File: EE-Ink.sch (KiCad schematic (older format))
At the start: 12 parts

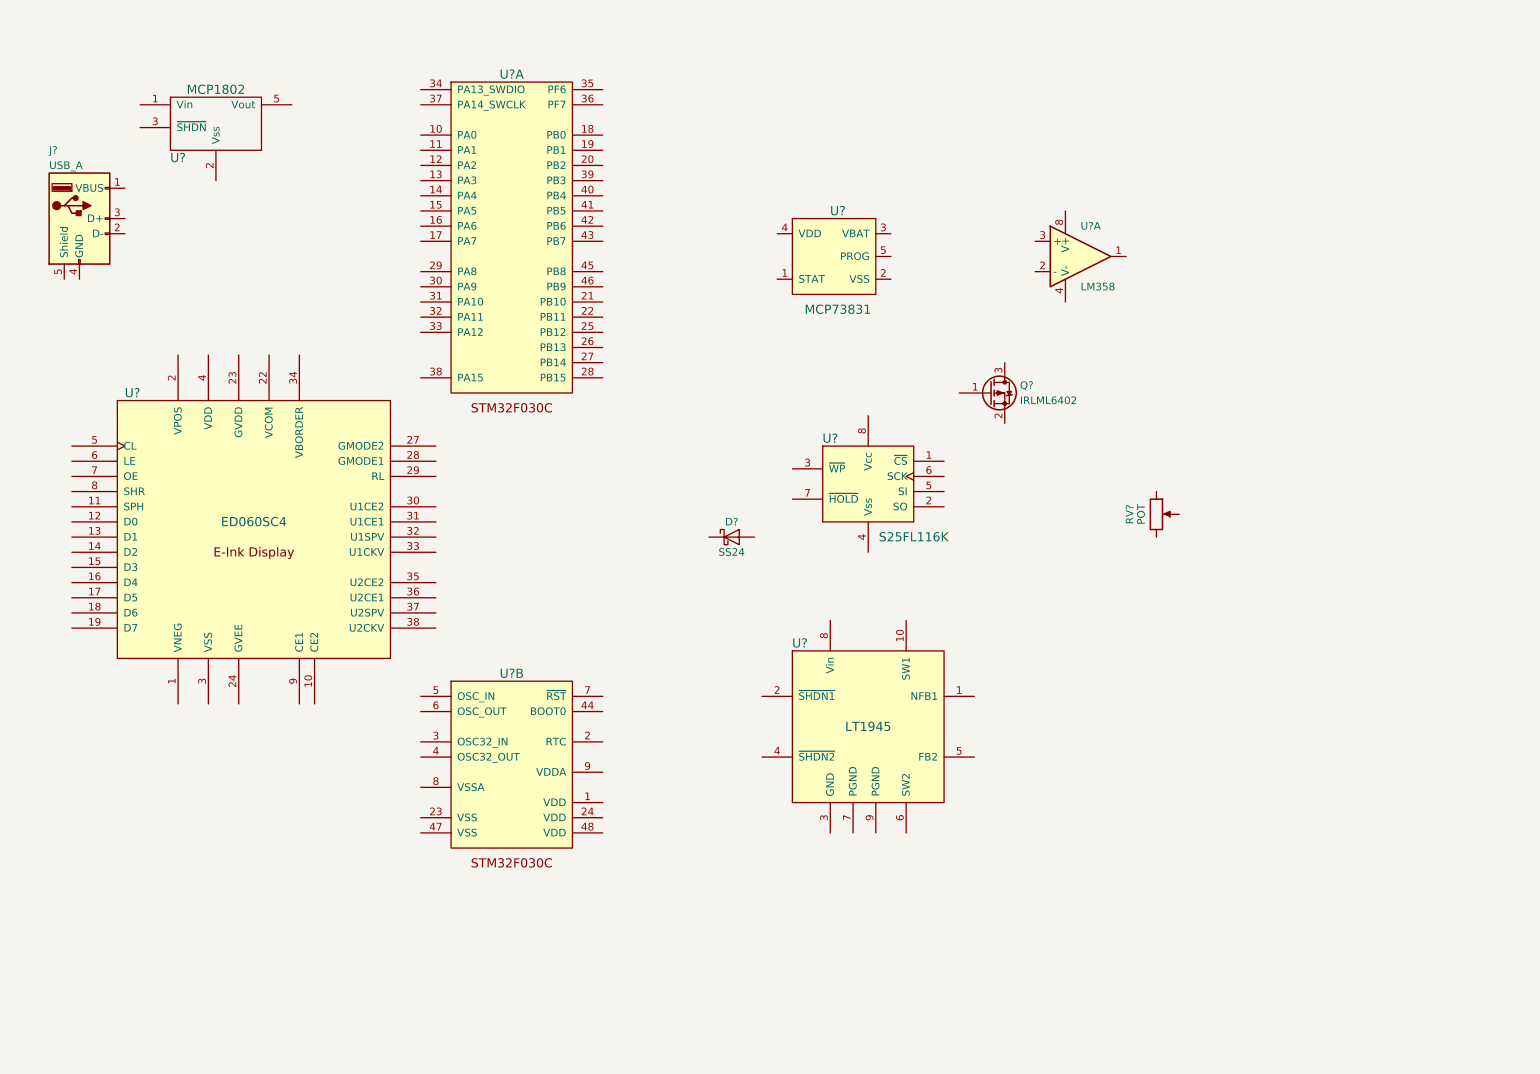
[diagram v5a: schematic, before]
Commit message: Began creating connections in the schematic.
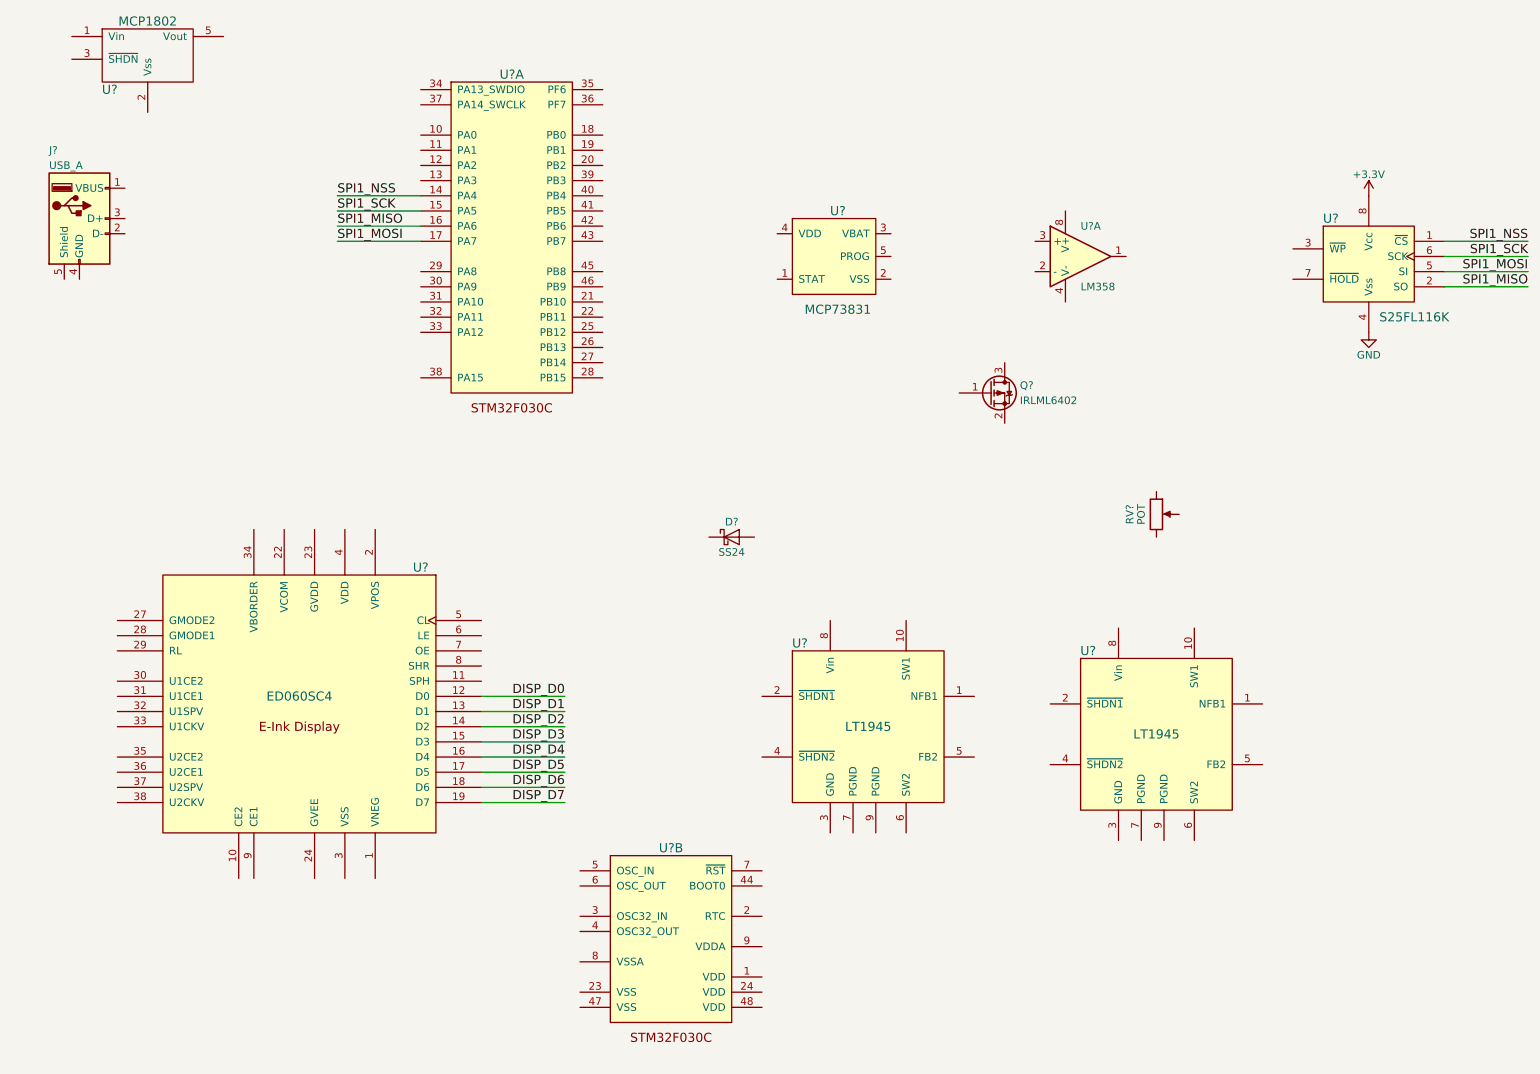
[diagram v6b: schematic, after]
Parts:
- added U?: LT1945, symbol LT1945
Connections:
- net SPI1_NSS: now reaches U?.14 (PA4)
- net SPI1_NSS: now also U?.1 (~CS)
- net SPI1_SCK: now reaches U?.15 (PA5)
- net SPI1_SCK: now also U?.6 (SCK)
- net SPI1_MISO: now reaches U?.16 (PA6)
- net SPI1_MISO: now also U?.2 (SO)
- net SPI1_MOSI: now reaches U?.17 (PA7)
- net SPI1_MOSI: now also U?.5 (SI)
- net GND: now reaches U?.4 (Vss)
- net +3V3: now reaches U?.8 (Vcc)
- net DISP_D0: now reaches U?.12 (D0)
- net DISP_D1: now reaches U?.13 (D1)
- net DISP_D2: now reaches U?.14 (D2)
- net DISP_D3: now reaches U?.15 (D3)
- net DISP_D4: now reaches U?.16 (D4)
- net DISP_D5: now reaches U?.17 (D5)
- net DISP_D6: now reaches U?.18 (D6)
- net DISP_D7: now reaches U?.19 (D7)
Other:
- moved on the sheet: U?, U?B
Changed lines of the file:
@@
 L STM32F030C U?
 U 2 1 58D6D1AF
-P 3950 6100
-F 0 "U?" H 3950 7000 60  0000 C CNN
-F 1 "STM32F030C" H 3950 4700 60  0001 C CNN
-F 2 "" H 2350 5950 60  0000 C CNN
-F 3 "" H 2350 5950 60  0000 C CNN
-	2    3950 6100
+P 5000 7250
+F 0 "U?" H 5000 8150 60  0000 C CNN
+F 1 "STM32F030C" H 5000 5850 60  0001 C CNN
+F 2 "" H 3400 7100 60  0000 C CNN
+F 3 "" H 3400 7100 60  0000 C CNN
+	2    5000 7250
 	1    0    0    -1
 $EndComp
@@
 L S25FL1xxK U?
 U 1 1 58D6DCDF
-P 6300 3950
-F 0 "U?" H 6050 4250 60  0000 C CNN
-F 1 "S25FL116K" H 6600 3600 60  0000 C CNN
-F 2 "" H 6200 4000 60  0001 C CNN
-F 3 "" H 6200 4000 60  0001 C CNN
-	1    6300 3950
+P 9600 2500
+F 0 "U?" H 9350 2800 60  0000 C CNN
+F 1 "S25FL116K" H 9900 2150 60  0000 C CNN
+F 2 "" H 9500 2550 60  0001 C CNN
+F 3 "" H 9500 2550 60  0001 C CNN
+	1    9600 2500
 	1    0    0    -1
 $EndComp
@@
 L ED060SC4 U?
 U 1 1 58D7DC1F
-P 2250 4250
-F 0 "U?" H 1450 5150 60  0000 C CNN
-F 1 "ED060SC4" H 2250 4300 60  0000 C CNN
-F 2 "" H 2250 4250 60  0000 C CNN
-F 3 "" H 2250 4250 60  0000 C CNN
-	1    2250 4250
-	1    0    0    -1
+P 2550 5400
+F 0 "U?" H 1750 6300 60  0000 C CNN
+F 1 "ED060SC4" H 2550 5450 60  0000 C CNN
+F 2 "" H 2550 5400 60  0000 C CNN
+F 3 "" H 2550 5400 60  0000 C CNN
+	1    2550 5400
+	-1   0    0    -1
 $EndComp
 $Comp
@@
 L MCP1802 U?
 U 1 1 58D83813
-P 2000 1550
-F 0 "U?" H 1750 1300 60  0000 C CNN
-F 1 "MCP1802" H 2000 1750 60  0000 C CNN
-F 2 "" H 2000 1850 60  0001 C CNN
-F 3 "" H 2000 1850 60  0001 C CNN
-	1    2000 1550
-	1    0    0    -1
-$EndComp
+P 1550 1100
+F 0 "U?" H 1300 850 60  0000 C CNN
+F 1 "MCP1802" H 1550 1300 60  0000 C CNN
+F 2 "" H 1550 1400 60  0001 C CNN
+F 3 "" H 1550 1400 60  0001 C CNN
+	1    1550 1100
+	1    0    0    -1
+$EndComp
+Wire Wire Line
+	3750 5450 4300 5450
+Wire Wire Line
+	3750 5550 4300 5550
+Wire Wire Line
+	3750 5650 4300 5650
+Wire Wire Line
+	3750 5750 4300 5750
+Wire Wire Line
+	3750 5850 4300 5850
+Wire Wire Line
+	3750 5950 4300 5950
+Wire Wire Line
+	3750 6050 4300 6050
+Wire Wire Line
+	3750 5350 4300 5350
+Text Label 4300 5350 2    60   ~ 0
+DISP_D0
+Text Label 4300 5450 2    60   ~ 0
+DISP_D1
+Text Label 4300 5550 2    60   ~ 0
+DISP_D2
+Text Label 4300 5650 2    60   ~ 0
+DISP_D3
+Text Label 4300 5750 2    60   ~ 0
+DISP_D4
+Text Label 4300 5850 2    60   ~ 0
+DISP_D5
+Text Label 4300 5950 2    60   ~ 0
+DISP_D6
+Text Label 4300 6050 2    60   ~ 0
+DISP_D7
+Wire Wire Line
+	2800 2350 3350 2350
+Wire Wire Line
+	2800 2250 3350 2250
+Wire Wire Line
+	2800 2150 3350 2150
+Wire Wire Line
+	2800 2050 3350 2050
+Text Label 2800 2050 0    60   ~ 0
+SPI1_NSS
+Text Label 2800 2150 0    60   ~ 0
+SPI1_SCK
+Text Label 2800 2250 0    60   ~ 0
+SPI1_MISO
+Text Label 2800 2350 0    60   ~ 0
+SPI1_MOSI
+$Comp
+L GND #PWR?
+U 1 1 58D85C6E
+P 9600 2950
+F 0 "#PWR?" H 9600 2700 50  0001 C CNN
+F 1 "GND" H 9600 2800 50  0000 C CNN
+F 2 "" H 9600 2950 50  0001 C CNN
+F 3 "" H 9600 2950 50  0001 C CNN
+	1    9600 2950
+	1    0    0    -1
+$EndComp
+$Comp
+L +3.3V #PWR?
+U 1 1 58D85C9A
+P 9600 2050
+F 0 "#PWR?" H 9600 1900 50  0001 C CNN
+F 1 "+3.3V" H 9600 2190 50  0000 C CNN
+F 2 "" H 9600 2050 50  0001 C CNN
+F 3 "" H 9600 2050 50  0001 C CNN
+	1    9600 2050
+	1    0    0    -1
+$EndComp
+Text Label 10650 2350 2    60   ~ 0
+SPI1_NSS
+Wire Wire Line
+	10650 2350 10100 2350
+Text Label 10650 2450 2    60   ~ 0
+SPI1_SCK
+Text Label 10650 2650 2    60   ~ 0
+SPI1_MISO
+Text Label 10650 2550 2    60   ~ 0
+SPI1_MOSI
+Wire Wire Line
+	10650 2650 10100 2650
+Wire Wire Line
+	10100 2550 10650 2550
+Wire Wire Line
+	10650 2450 10100 2450
+$Comp
+L LT1945 U?
+U 1 1 58D8A2B0
+P 8200 5600
+F 0 "U?" H 7750 6150 60  0000 C CNN
+F 1 "LT1945" H 8200 5600 60  0000 C CNN
+F 2 "" H 8200 5600 60  0001 C CNN
+F 3 "" H 8200 5600 60  0001 C CNN
+	1    8200 5600
+	1    0    0    -1
+$EndComp

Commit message: Connected all wires to E-ink component.
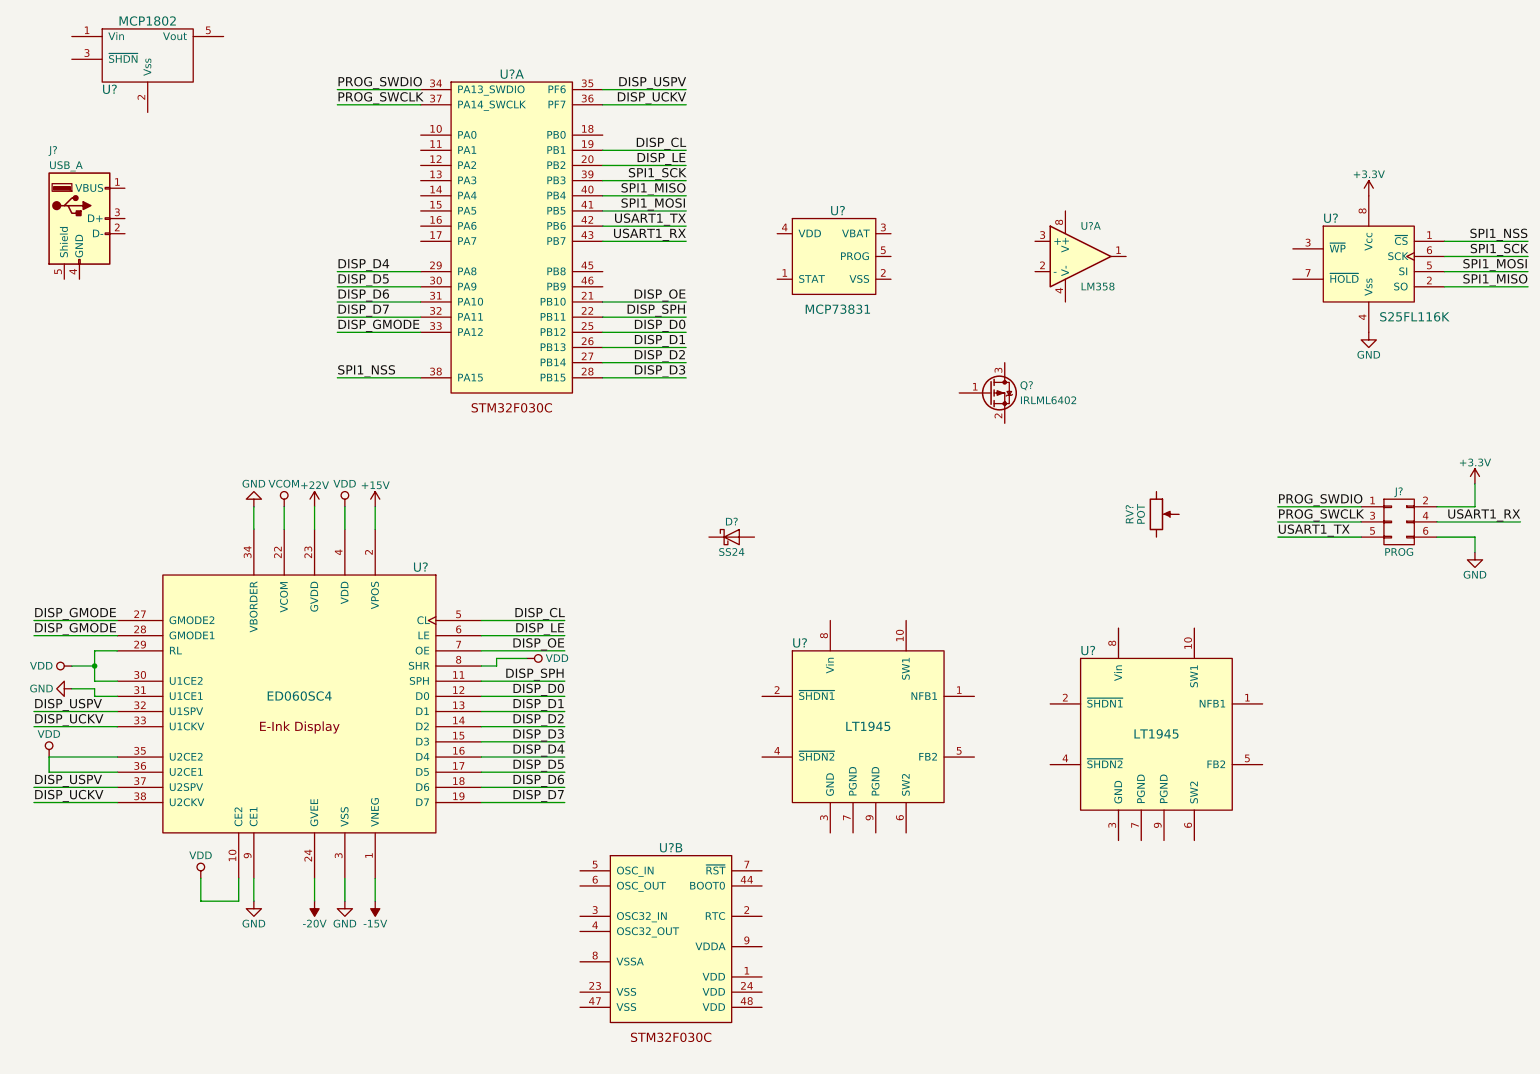
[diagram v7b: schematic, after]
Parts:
- added J?: PROG, symbol CONN_02X03
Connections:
- net +3V3: now also J?.2 (P2)
- net DISP_D0: now also U?.25 (PB12)
- net DISP_D1: now also U?.26 (PB13)
- net DISP_D2: now also U?.27 (PB14)
- net DISP_D3: now also U?.28 (PB15)
- net DISP_D4: now also U?.29 (PA8)
- net DISP_D5: now also U?.30 (PA9)
- net DISP_D6: now also U?.31 (PA10)
- net DISP_D7: now also U?.32 (PA11)
- net GND: now also U?.3 (VSS), U?.31 (U1CE1), U?.34 (VBORDER), U?.9 (CE1), J?.6 (P6)
- net SPI1_MISO: now also U?.40 (PB4); no longer U?.16 (PA6)
- net SPI1_MOSI: now also U?.41 (PB5); no longer U?.17 (PA7)
- net SPI1_NSS: now also U?.38 (PA15); no longer U?.14 (PA4)
- net SPI1_SCK: now also U?.39 (PB3); no longer U?.15 (PA5)
- net DISP_CL: now reaches U?.19 (PB1)
- net DISP_CL: now also U?.5 (CL)
- net DISP_LE: now reaches U?.20 (PB2)
- net DISP_LE: now also U?.6 (LE)
- net DISP_OE: now reaches U?.21 (PB10)
- net DISP_OE: now also U?.7 (OE)
- net DISP_SPH: now reaches U?.22 (PB11)
- net DISP_SPH: now also U?.11 (SPH)
- net DISP_GMODE: now reaches U?.33 (PA12)
- net DISP_GMODE: now also U?.27 (GMODE2), U?.28 (GMODE1)
- net PROG_SWDIO: now reaches U?.34 (PA13_SWDIO)
- net PROG_SWDIO: now also J?.1 (P1)
- net DISP_USPV: now reaches U?.35 (PF6)
- net DISP_USPV: now also U?.32 (U1SPV), U?.37 (U2SPV)
- net DISP_UCKV: now reaches U?.36 (PF7)
- net DISP_UCKV: now also U?.33 (U1CKV), U?.38 (U2CKV)
- net PROG_SWCLK: now reaches U?.37 (PA14_SWCLK)
- net PROG_SWCLK: now also J?.3 (P3)
- net USART1_TX: now reaches U?.42 (PB6)
- net USART1_TX: now also J?.5 (P5)
- net USART1_RX: now reaches U?.43 (PB7)
- net USART1_RX: now also J?.4 (P4)
- net -15V: now reaches U?.1 (VNEG)
- net VDD: now reaches U?.10 (CE2)
- net VDD: now also U?.29 (RL), U?.30 (U1CE2), U?.35 (U2CE2), U?.36 (U2CE1), U?.4 (VDD), U?.8 (SHR)
- net +15V: now reaches U?.2 (VPOS)
- net VCOM: now reaches U?.22 (VCOM)
- net +22V: now reaches U?.23 (GVDD)
- net -20V: now reaches U?.24 (GVEE)
